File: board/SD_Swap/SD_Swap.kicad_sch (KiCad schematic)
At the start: 46 parts, among them J1 USB_C, Q1 Q_Dual_PNP_PNP_E1B1C2E2B2C1, U1 74LVC2G14, U2 RTS5306E, U3 PCB_SD, U4 93AAxxAT, U5 TS3A27518ERTW, U6 SD_SOCKET, U7 AP2127N-3.3, Y1 12MHz

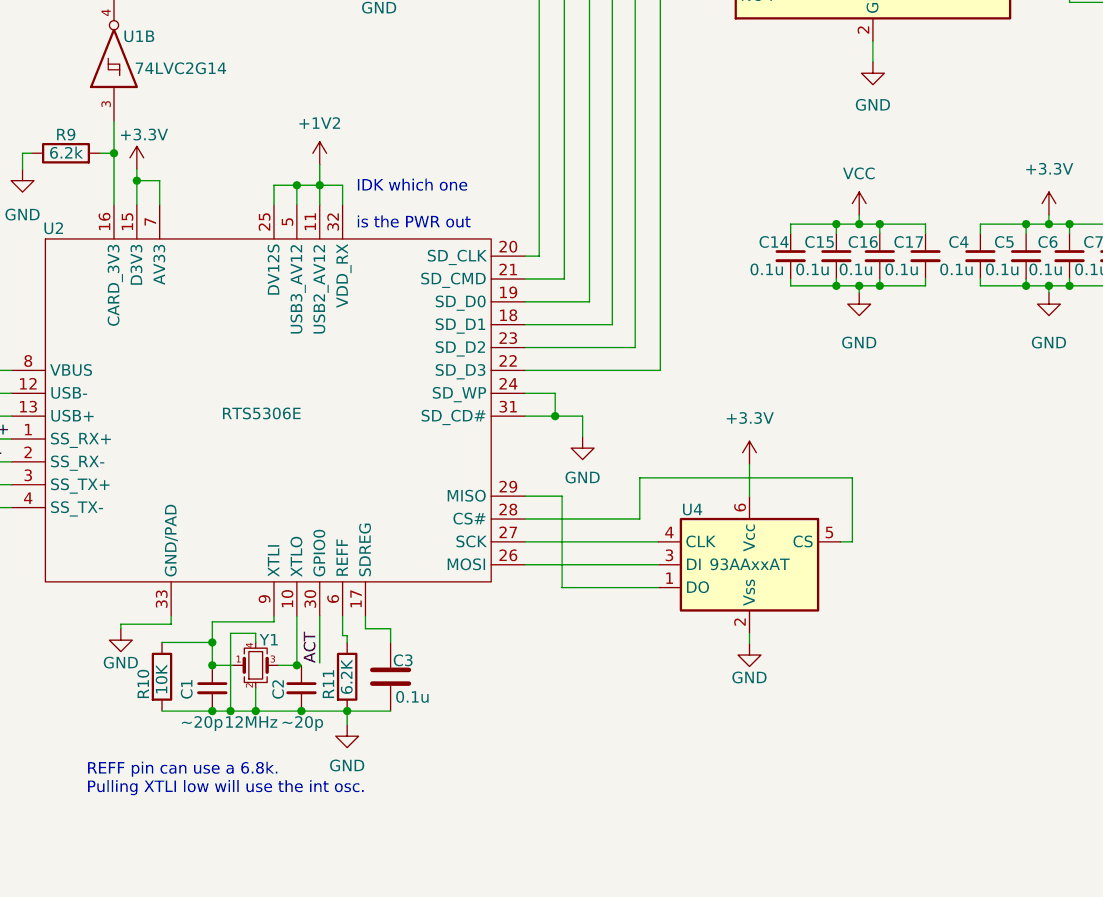
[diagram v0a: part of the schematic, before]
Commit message: more routing change osc and remove extra cap
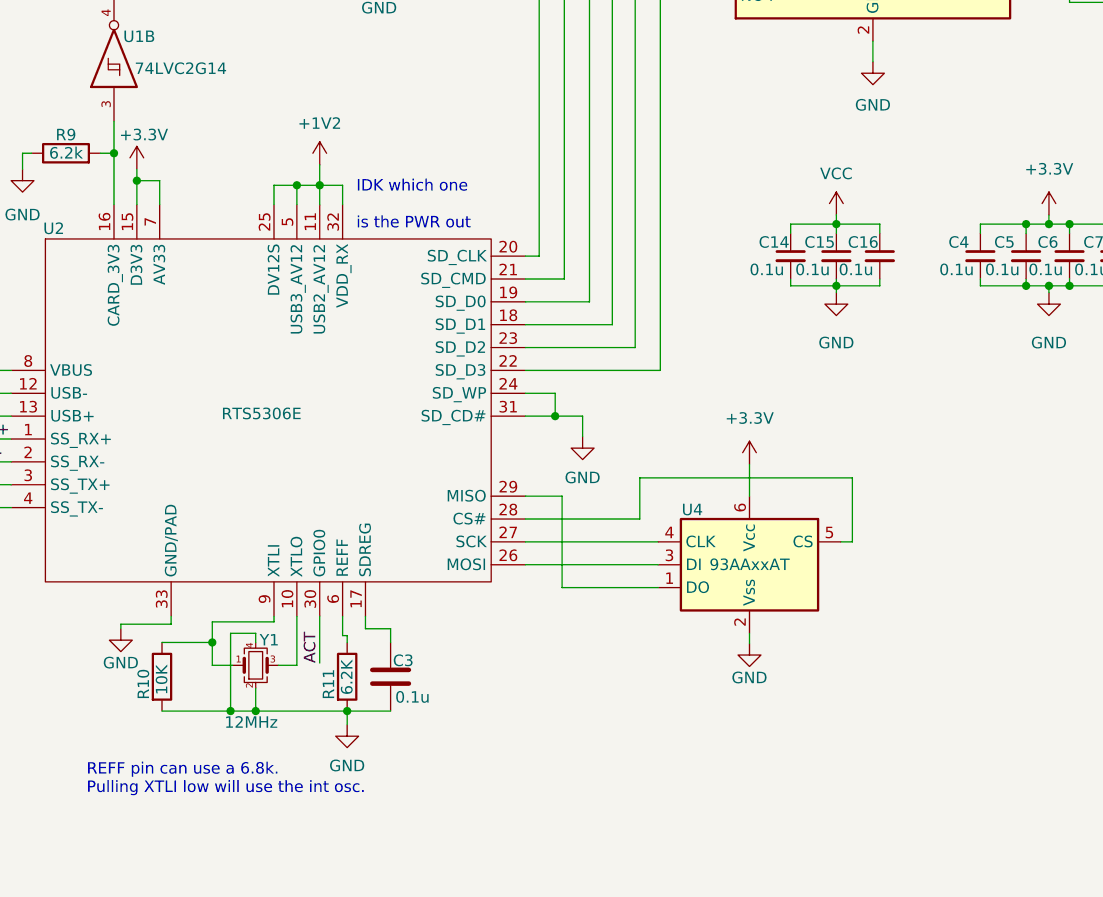
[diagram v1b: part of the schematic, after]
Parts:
- removed C1: ~20p, SD_Swap:105162-0001, symbol Device:C_Small
- removed C17: 0.1u, Capacitor_SMD:C_0201_0603Metric, symbol Device:C_Small
- removed C2: ~20p, Capacitor_SMD:C_0603_1608Metric, symbol Device:C_Small
- Y1: footprint Crystal:Crystal_SMD_Abracon_ABM8G-4Pin_3.2x2.5mm -> SD_Swap:Resonator-3.2x1.3mm

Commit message: BOM
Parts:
- C10, C11, C12, C14, C15, C16, C18, C19, C3, C4, C5, C6, C7, C8, C9: LCSC (none) -> C66938
- C13: LCSC (none) -> C107372
- D1: LCSC (none) -> C253534
- D2: LCSC (none) -> C264332
- D3: LCSC (none) -> C434419
- J1: Part Number (none) -> 12401548E4
- JP1, JP2, JP3, U3: Part Number (none) -> NONE
- Q1: LCSC (none) -> NONE; Part Number (none) -> QST8TR
- R1, R2, R3: LCSC (none) -> C4260
- R11: LCSC (none) -> C423334
- R4, R5: LCSC (none) -> C100142
- R6, R7: LCSC (none) -> C138165
- R8, R9: value 6.2k -> 6.2K; LCSC (none) -> C423334
- U1: LCSC (none) -> C12401; Part Number (none) -> 74LVC2G14
- U2: LCSC (none) -> C2848856; Part Number (none) -> RTS5306E
- U4: Part Number (none) -> 93AA86AT
- U5: LCSC (none) -> C2651937; Part Number (none) -> TS3A27518ERTW
- U6: Part Number (none) -> 105162-0001
- U7: LCSC (none) -> C176954; Part Number (none) -> AP2127N-3.3
- Y1: LCSC (none) -> C907940; Part Number (none) -> CSTNE12M0G55A000R0

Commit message: update BOM
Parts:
- J1: LCSC (none) -> C2835314
- Q1: LCSC NONE -> C703623
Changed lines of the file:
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@@
       (effects (font (size 1.27 1.27)) hide)
     )
-    (property "LCSC" "" (id 4) (at 124.968 142.748 0)
+    (property "LCSC" "~" (id 4) (at 124.968 142.748 0)
       (effects (font (size 1.27 1.27)) hide)
     )
@@
       (effects (font (size 1.27 1.27)) hide)
     )
-    (property "LCSC" "NONE" (id 4) (at 93.218 23.622 0)
+    (property "LCSC" "C703623" (id 4) (at 93.218 23.622 0)
       (effects (font (size 1.27 1.27)) hide)
     )
@@
       (effects (font (size 1.27 1.27)) hide)
     )
-    (property "LCSC" "NONE" (id 4) (at 109.728 23.622 0)
+    (property "LCSC" "C703623" (id 4) (at 109.728 23.622 0)
       (effects (font (size 1.27 1.27)) hide)
     )
@@
       (effects (font (size 1.27 1.27)) hide)
     )
-    (property "LCSC" "~" (id 4) (at 27.686 148.082 0)
-      (effects (font (size 1.27 1.27)) hide)
-    )
+    (property "LCSC" "C2835314" (id 4) (at 27.686 148.082 0)
+      (effects (font (size 1.27 1.27)) hide)
+    )

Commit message: update fix led
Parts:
- J1: LCSC C2835314 -> C3197851
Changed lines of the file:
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@@
       (effects (font (size 1.27 1.27)) hide)
     )
-    (property "LCSC" "C2835314" (id 4) (at 27.686 148.082 0)
+    (property "LCSC" "C3197851" (id 4) (at 27.686 148.082 0)
       (effects (font (size 1.27 1.27)) hide)
     )

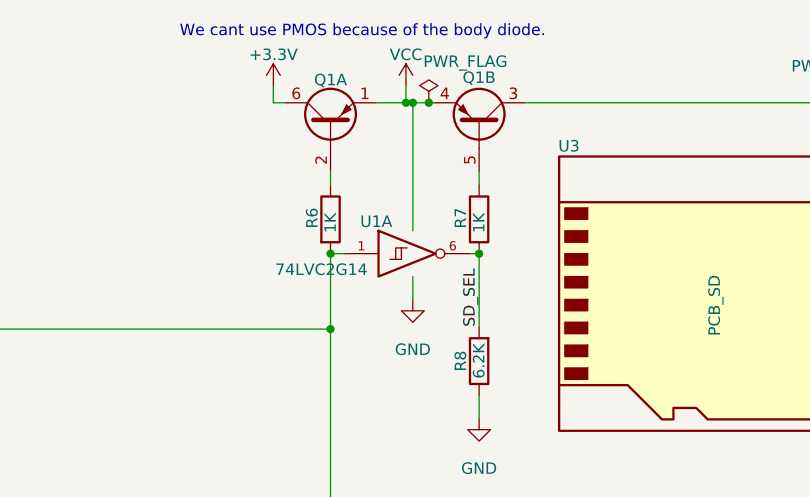
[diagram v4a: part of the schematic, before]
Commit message: fixed clearance issue pnp base resistor is now 100R
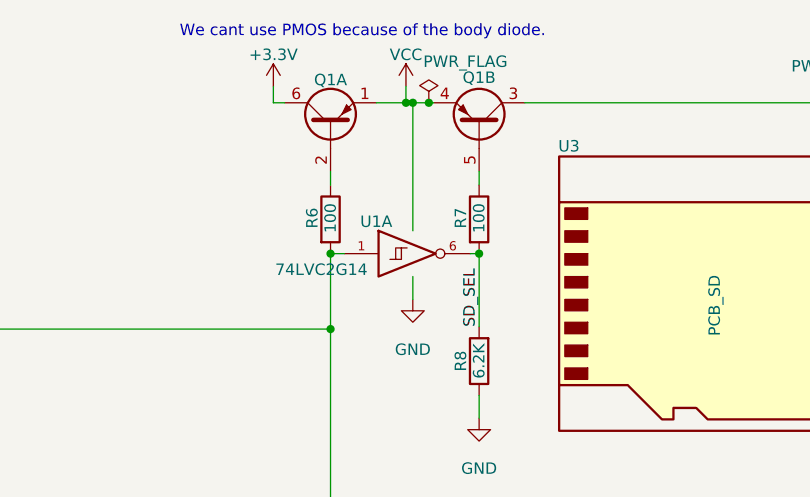
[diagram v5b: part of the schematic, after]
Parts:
- R6, R7: value 1K -> 100
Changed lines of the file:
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@@
       (effects (font (size 1.27 1.27)) (justify left))
     )
-    (property "Value" "1K" (id 1) (at 93.218 35.56 90)
+    (property "Value" "100" (id 1) (at 93.218 35.56 90)
       (effects (font (size 1.27 1.27)) (justify left))
     )
@@
       (effects (font (size 1.27 1.27)) (justify left))
     )
-    (property "Value" "1K" (id 1) (at 109.728 35.56 90)
+    (property "Value" "100" (id 1) (at 109.728 35.56 90)
       (effects (font (size 1.27 1.27)) (justify left))
     )
@@
     )
     (path "/9f30e678-6f34-4642-bc78-e85ee3c895b5"
-      (reference "R6") (unit 1) (value "1K") (footprint "Resistor_SMD:R_0201_0603Metric")
+      (reference "R6") (unit 1) (value "100") (footprint "Resistor_SMD:R_0201_0603Metric")
     )
     (path "/d22c7432-0922-4a7c-b63e-13d7acc6d83d"
-      (reference "R7") (unit 1) (value "1K") (footprint "Resistor_SMD:R_0201_0603Metric")
+      (reference "R7") (unit 1) (value "100") (footprint "Resistor_SMD:R_0201_0603Metric")
     )
     (path "/31176b82-3897-4c98-9a3b-41de27815692"

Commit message: update sch
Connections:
- net +3.3V: now also Q1.1 (E1); no longer Q1.6 (C1)
- net VCC: now also Q1.3 (C2), Q1.6 (C1); no longer Q1.1 (E1), Q1.4 (E2)
- net at U3.4 (VDD): now also Q1.4 (E2); no longer Q1.3 (C2)
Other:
- note added: "For 100R use BJT with Hfe>260. 260*3.3/100=8.58"
- note removed: "All parts running off SD power must work in the range of 1.7-3.6 per SD spec"
- moved on the sheet: Q1A, Q1B
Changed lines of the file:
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@@
-    (effects (font (size 1.27 1.27)) (justify left bottom))
-  )
-  (text "All parts running off SD power must work\nin the range of 1.7-3.6 per SD spec"
-    (at 65.024 84.328 0)
     (effects (font (size 1.27 1.27)) (justify left bottom))
   )
@@
   (text "REFF pin can use a 6.8k.\nPulling XTLI low will use the int osc."
     (at 116.586 155.956 0)
+    (effects (font (size 1.27 1.27)) (justify left bottom))
+  )
+  (text "For 100R use BJT with Hfe>260.\n260*3.3/100=8.58\n" (at 58.674 29.337 0)
     (effects (font (size 1.27 1.27)) (justify left bottom))
   )
@@
     (pin "1")
   )
-  (symbol (lib_id "Device:Q_Dual_PNP_PNP_E1B1C2E2B2C1") (at 93.218 23.622 90) (unit 1)
+  (symbol (lib_id "Device:Q_Dual_PNP_PNP_E1B1C2E2B2C1") (at 93.218 23.622 270) (mirror x) (unit 1)
     (in_bom yes) (on_board yes)
     (property "Reference" "Q1" (id 0) (at 93.218 18.542 90))
-    (property "Value" "Q_Dual_PNP_PNP_E1B1C2E2B2C1" (id 1) (at 113.03 19.05 90)
-      (effects (font (size 1.27 1.27)) hide)
-    )
-    (property "Footprint" "Package_TO_SOT_SMD:SOT-23-6" (id 2) (at 90.678 18.542 0)
+    (property "Value" "Q_Dual_PNP_PNP_E1B1C2E2B2C1" (id 1) (at 73.406 19.05 90)
+      (effects (font (size 1.27 1.27)) hide)
+    )
+    (property "Footprint" "Package_TO_SOT_SMD:SOT-23-6" (id 2) (at 95.758 18.542 0)
       (effects (font (size 1.27 1.27)) hide)
     )
@@
     (pin "2")
   )
-  (symbol (lib_id "Device:Q_Dual_PNP_PNP_E1B1C2E2B2C1") (at 109.728 23.622 270) (mirror x) (unit 2)
+  (symbol (lib_id "Device:Q_Dual_PNP_PNP_E1B1C2E2B2C1") (at 109.728 23.622 90) (unit 2)
     (in_bom yes) (on_board yes)
     (property "Reference" "Q1" (id 0) (at 109.728 18.288 90))
-    (property "Value" "Q_Dual_PNP_PNP_E1B1C2E2B2C1" (id 1) (at 92.456 26.416 90)
-      (effects (font (size 1.27 1.27)) hide)
-    )
-    (property "Footprint" "Package_TO_SOT_SMD:SOT-23-6" (id 2) (at 112.268 18.542 0)
-      (effects (font (size 1.27 1.27)) hide)
-    )
+    (property "Value" "Q_Dual_PNP_PNP_E1B1C2E2B2C1" (id 1) (at 127 26.416 90)
+      (effects (font (size 1.27 1.27)) hide)
+    )
+    (property "Footprint" "Package_TO_SOT_SMD:SOT-23-6" (id 2) (at 107.188 18.542 0)
+      (effects (font (size 1.27 1.27)) hide)
+    )

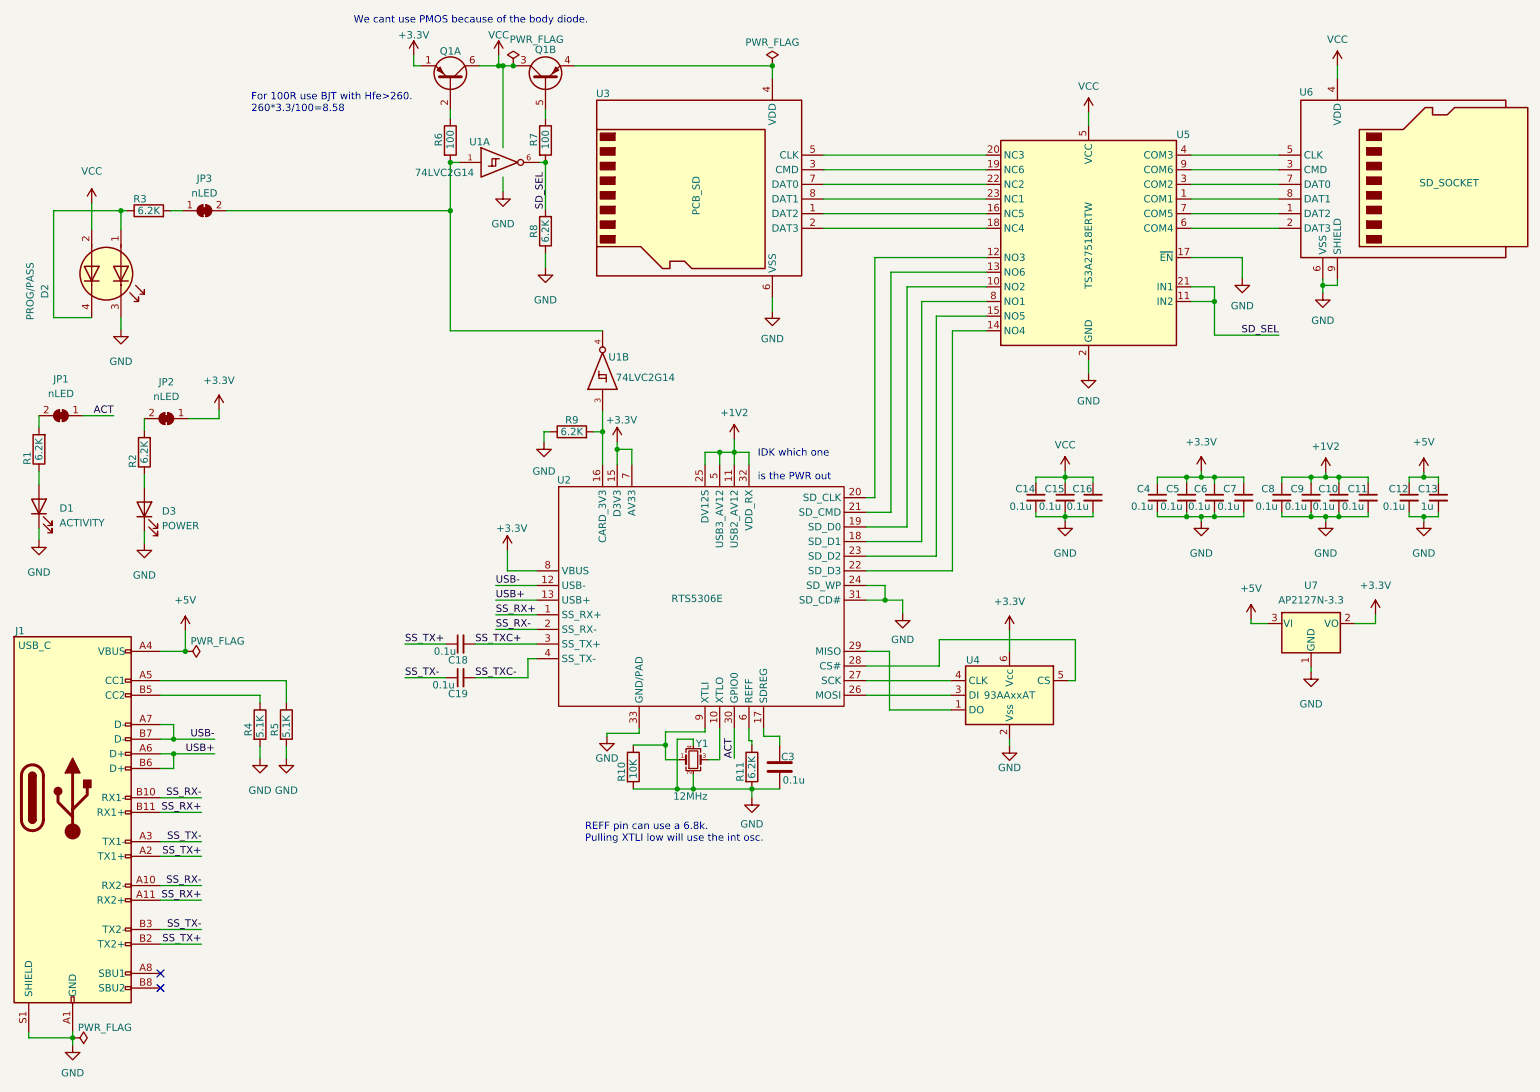
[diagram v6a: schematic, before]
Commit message: add bigger reg to sch, update BOM,update todo
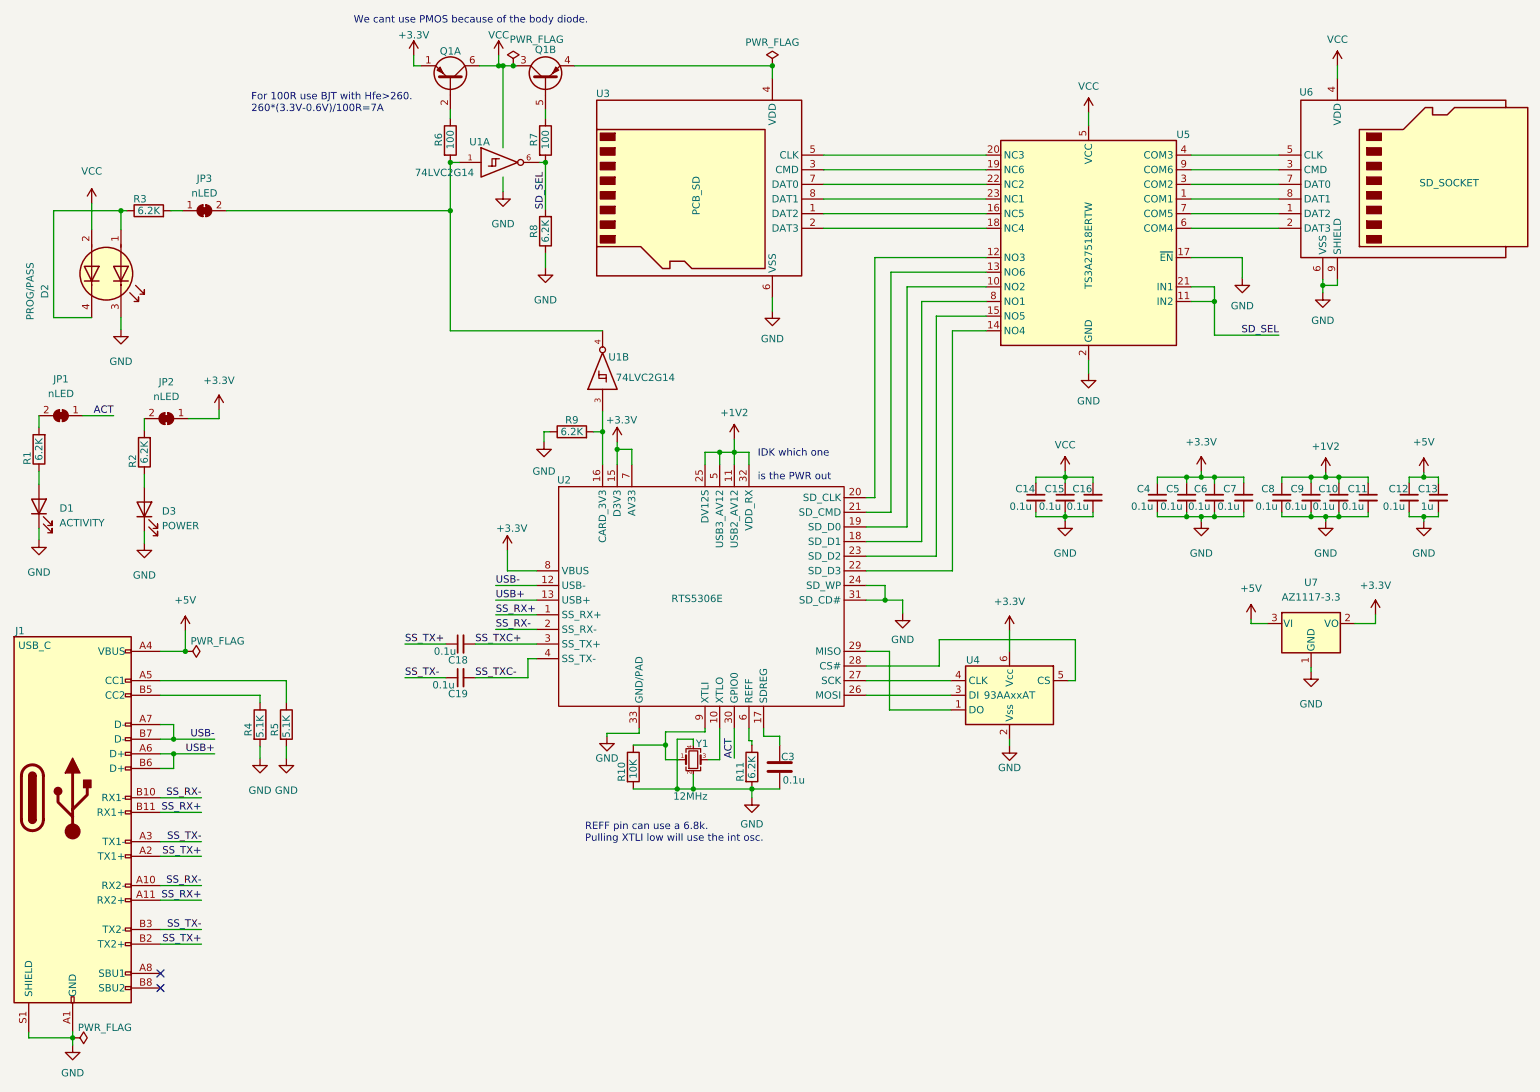
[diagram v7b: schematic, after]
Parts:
- removed U7: AP2127N-3.3, Package_TO_SOT_SMD:SOT-23, symbol Regulator_Linear:AP2127N-3.3
- added U7: AZ1117-3.3, Package_TO_SOT_SMD:SOT-223-3_TabPin2, symbol Regulator_Linear:AZ1117-3.3
- R6, R7: LCSC C138165 -> C2991668
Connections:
- net +3.3V: now also U7.2 (VO)
- net +5V: now also U7.3 (VI)
- net GND: now also U7.1 (GND)
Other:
- note added: "For 100R use BJT with Hfe>260. 260*(3.3V-0.6V)/100R=7A"
- note removed: "For 100R use BJT with Hfe>260. 260*3.3/100=8.58"
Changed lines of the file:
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@@
     (effects (font (size 1.27 1.27)) (justify left bottom))
   )
-  (text "For 100R use BJT with Hfe>260.\n260*3.3/100=8.58\n" (at 58.674 29.337 0)
+  (text "For 100R use BJT with Hfe>260.\n260*(3.3V-0.6V)/100R=7A\n"
+    (at 58.674 29.337 0)
     (effects (font (size 1.27 1.27)) (justify left bottom))
   )
@@
       (effects (font (size 1.27 1.27)) hide)
     )
-    (property "LCSC" "C138165" (id 4) (at 93.218 34.036 0)
+    (property "LCSC" "C2991668" (id 4) (at 93.218 34.036 0)
       (effects (font (size 1.27 1.27)) hide)
     )
@@
     (pin "1")
     (pin "2")
-  )
-  (symbol (lib_id "Regulator_Linear:AP2127N-3.3") (at 242.57 117.856 0) (unit 1)
-    (in_bom yes) (on_board yes) (fields_autoplaced)
-    (property "Reference" "U7" (id 0) (at 242.57 111.252 0))
-    (property "Value" "AP2127N-3.3" (id 1) (at 242.57 113.792 0))
-    (property "Footprint" "Package_TO_SOT_SMD:SOT-23" (id 2) (at 242.57 112.141 0)
-      (effects (font (size 1.27 1.27) italic) hide)
-    )
-    (property "Datasheet" "https://www.diodes.com/assets/Datasheets/AP2127.pdf" (id 3) (at 242.57 117.856 0)
-      (effects (font (size 1.27 1.27)) hide)
-    )
-    (property "LCSC" "C176954" (id 4) (at 242.57 117.856 0)
-      (effects (font (size 1.27 1.27)) hide)
-    )
-    (property "Part Number" "AP2127N-3.3" (id 5) (at 242.57 117.856 0)
-      (effects (font (size 1.27 1.27)) hide)
-    )
-    (pin "1")
-    (pin "2")
-    (pin "3")
   )
   (symbol (lib_id "power:+3.3V") (at 122.174 86.36 0) (unit 1)
@@
     (pin "1")
     (pin "2")
+  )
+  (symbol (lib_id "Regulator_Linear:AZ1117-3.3") (at 242.57 117.856 0) (unit 1)
+    (in_bom yes) (on_board yes) (fields_autoplaced)
+    (property "Reference" "U7" (id 0) (at 242.57 110.744 0))
+    (property "Value" "AZ1117-3.3" (id 1) (at 242.57 113.284 0))
+    (property "Footprint" "Package_TO_SOT_SMD:SOT-223-3_TabPin2" (id 2) (at 242.57 111.506 0)
+      (effects (font (size 1.27 1.27) italic) hide)
+    )
+    (property "Datasheet" "https://www.diodes.com/assets/Datasheets/AZ1117.pdf" (id 3) (at 242.57 117.856 0)
+      (effects (font (size 1.27 1.27)) hide)
+    )
+    (property "LCSC" "C92102" (id 4) (at 242.57 117.856 0)
+      (effects (font (size 1.27 1.27)) hide)
+    )
+    (property "Part Number" "AZ1117CH-3.3TRG1" (id 5) (at 242.57 117.856 0)
+      (effects (font (size 1.27 1.27)) hide)
+    )
+    (pin "1")
+    (pin "2")
+    (pin "3")
   )
   (symbol (lib_id "power:+5V") (at 262.128 91.694 0) (unit 1)
@@
       (effects (font (size 1.27 1.27)) hide)
     )
-    (property "LCSC" "C138165" (id 4) (at 109.728 34.036 0)
+    (property "LCSC" "C2991668" (id 4) (at 109.728 34.036 0)
       (effects (font (size 1.27 1.27)) hide)
     )
@@
       (reference "U6") (unit 1) (value "SD_SOCKET") (footprint "SD_Swap:105162-0001")
     )
-    (path "/9fc772fc-7a92-45cc-a80f-b1ab89f05f6f"
-      (reference "U7") (unit 1) (value "AP2127N-3.3") (footprint "Package_TO_SOT_SMD:SOT-23")
+    (path "/bc05b403-1d3d-493d-9019-c86b4674c7ab"
+      (reference "U7") (unit 1) (value "AZ1117-3.3") (footprint "Package_TO_SOT_SMD:SOT-223-3_TabPin2")
     )
     (path "/c3719856-7676-44b9-abe1-20dc98727834"
